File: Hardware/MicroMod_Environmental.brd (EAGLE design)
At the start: 65 x 38 mm, 41 parts, among them J1 MICROMOD_STANDARD, U1 SGP40, U2 EEPROM, U3 SHTC3, U4 3.3V, U5 STC31

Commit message: Adds Silk for default I2C address
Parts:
- added U$10: (no value), top:0X29518
- added U$9: (no value), top:DEFAULT#518
- moved C3 0.05 mm to (25.5, 21.8)
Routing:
- net GND: vias 21 -> 23
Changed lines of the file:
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@@
 <attribute name="VALUE" x="28.321" y="32.766" size="0.6096" layer="27" font="vector" ratio="20" align="top-center"/>
 </element>
-<element name="C3" library="SparkFun-Capacitors" package="0603" value="0.1uF" x="25.5016" y="21.7424" smashed="yes">
-<attribute name="NAME" x="25.5016" y="22.5044" size="0.6096" layer="25" font="vector" ratio="20" align="bottom-center"/>
-<attribute name="PROD_ID" value="CAP-08604" x="25.5016" y="26.8224" size="1.778" layer="27" font="vector" ratio="15" display="off"/>
-<attribute name="VALUE" x="25.5016" y="20.9804" size="0.6096" layer="27" font="vector" ratio="20" align="top-center"/>
+<element name="C3" library="SparkFun-Capacitors" package="0603" value="0.1uF" x="25.5016" y="21.7932" smashed="yes">
+<attribute name="NAME" x="25.5016" y="22.5552" size="0.6096" layer="25" font="vector" ratio="20" align="bottom-center"/>
+<attribute name="PROD_ID" value="CAP-08604" x="25.5016" y="26.8732" size="1.778" layer="27" font="vector" ratio="15" display="off"/>
+<attribute name="VALUE" x="25.5016" y="21.0312" size="0.6096" layer="27" font="vector" ratio="20" align="top-center"/>
 </element>
 <element name="U3" library="SparkFun-Sensors" package="SHTC3" value="SHTC3" x="32.893" y="19.05" smashed="yes" rot="R180">
@@
 <element name="U$7" library="SparkFun-MicroMod" package="MICROMOD_MI_LOGO_1" value="" x="39.116" y="32.512" smashed="yes"/>
 <element name="U$8" library="SparkFun-Buzzard" package="I2C" value="" x="8.001" y="8.255" smashed="yes"/>
+<element name="U$9" library="top" package="DEFAULT#518" value="" x="26.924" y="26.67" smashed="yes"/>
+<element name="U$10" library="top" package="0X29518" value="" x="31.115" y="26.67" smashed="yes"/>
 </elements>
 <signals>
@@
 <via x="43.5102" y="21.6408" extent="1-16" drill="0.3048"/>
 <via x="24.3586" y="17.1958" extent="1-16" drill="0.3048"/>
+<via x="40.5892" y="21.1582" extent="1-16" drill="0.3048"/>
+<via x="37.4142" y="17.018" extent="1-16" drill="0.3048"/>
 </signal>
 <signal name="3.3V" class="2">
@@
 <contactref element="PWR\" pad="2"/>
 <wire x1="32.893" y1="32.893" x2="55.118" y2="32.893" width="0.254" layer="1"/>
-<wire x1="24.6516" y1="21.7424" x2="24.384" y2="21.4748" width="0.3048" layer="1"/>
-<wire x1="24.384" y1="21.4748" x2="24.384" y2="20.828" width="0.3048" layer="1"/>
-<wire x1="24.384" y1="20.828" x2="24.384" y2="20.2" width="0.3048" layer="1"/>
-<wire x1="24.7904" y1="21.8812" x2="24.6516" y2="21.7424" width="0.3048" layer="1"/>
+<wire x1="24.6516" y1="21.7932" x2="24.384" y2="21.5256" width="0.3048" layer="1"/>
+<wire x1="24.384" y1="21.5256" x2="24.384" y2="20.8788" width="0.3048" layer="1"/>
+<wire x1="24.384" y1="20.8788" x2="24.384" y2="20.2" width="0.3048" layer="1"/>
+<wire x1="24.7904" y1="21.932" x2="24.6516" y2="21.7932" width="0.3048" layer="1"/>
 <wire x1="29.3624" y1="20.3454" x2="26.8224" y2="20.3454" width="0.3048" layer="16"/>
 <wire x1="26.8224" y1="20.3454" x2="24.6126" y2="20.3454" width="0.3048" layer="16"/>
@@
 <wire x1="39.3192" y1="18.0349" x2="39.5723" y2="18.288" width="0.3048" layer="1"/>
 <wire x1="39.5723" y1="18.288" x2="40.386" y2="18.288" width="0.3048" layer="1"/>
-<wire x1="24.384" y1="20.828" x2="24.384" y2="20.574" width="0.3048" layer="16"/>
-<via x="24.384" y="20.828" extent="1-16" drill="0.3048"/>
+<wire x1="24.384" y1="20.8788" x2="24.384" y2="20.574" width="0.3048" layer="16"/>
+<via x="24.384" y="20.8788" extent="1-16" drill="0.3048"/>
 <wire x1="24.6126" y1="20.3454" x2="24.384" y2="20.574" width="0.3048" layer="16"/>
 <wire x1="24.13" y1="27.178" x2="24.384" y2="26.924" width="0.3048" layer="16"/>
-<wire x1="24.384" y1="26.924" x2="24.384" y2="20.828" width="0.3048" layer="16"/>
+<wire x1="24.384" y1="26.924" x2="24.384" y2="20.8788" width="0.3048" layer="16"/>
 <via x="38.1" y="19.558" extent="1-16" drill="0.3048"/>
 <wire x1="29.3624" y1="20.3454" x2="30.1498" y2="19.558" width="0.3048" layer="16"/>

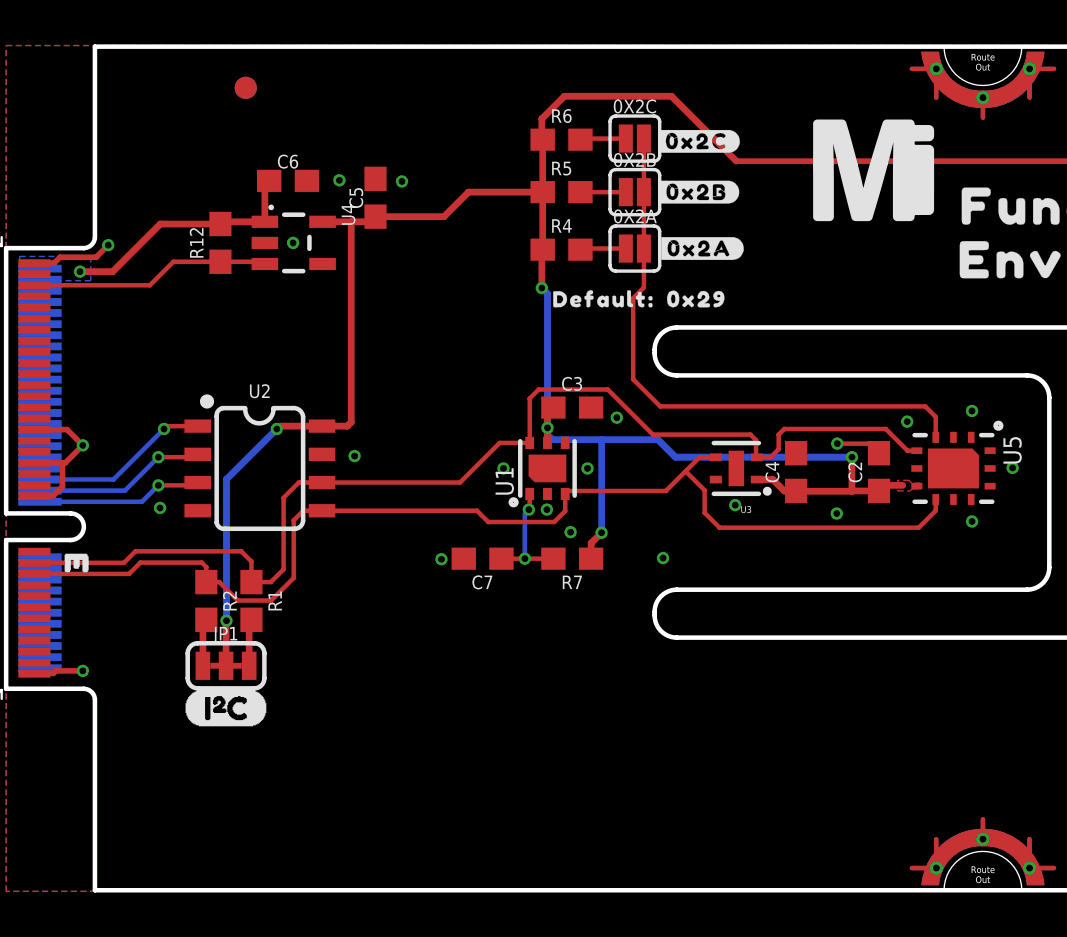
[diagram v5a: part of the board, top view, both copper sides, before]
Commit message: Adds some vias, moves some silk
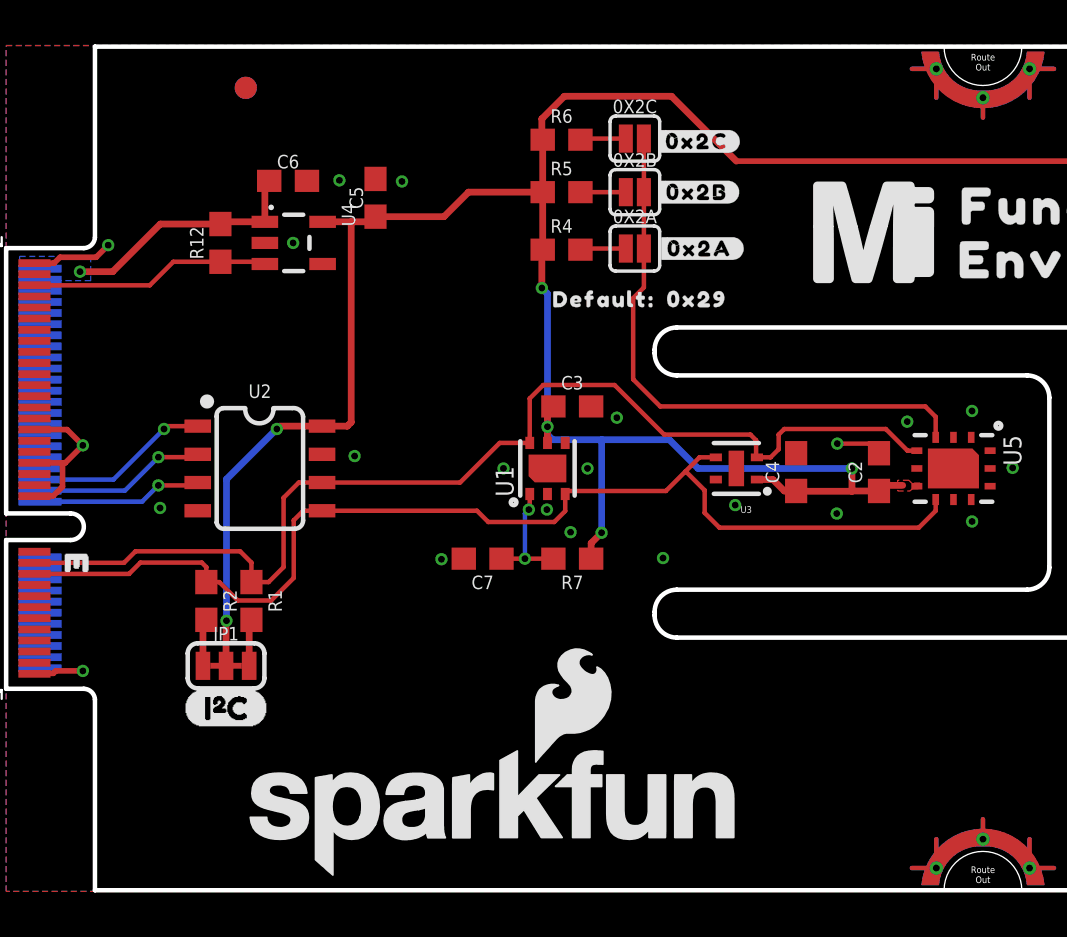
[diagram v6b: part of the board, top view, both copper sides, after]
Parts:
- moved U$7 2.79 mm to (39.1, 29.7)
- moved LOGO1 2.74 mm to (22.0, 3.56), flipped to the top
- moved C3 0.05 mm to (25.5, 21.8)
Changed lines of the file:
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@@
 <?xml version="1.0" encoding="utf-8"?>
 <!DOCTYPE eagle SYSTEM "eagle.dtd">
-<eagle version="9.6.2">
+<eagle version="9.5.1">
 <drawing>
 <settings>
@@
 <setting verticaltext="up"/>
 </settings>
-<grid distance="0.01" unitdist="inch" unit="inch" style="dots" multiple="1" display="yes" altdistance="0.001" altunitdist="inch" altunit="inch"/>
+<grid distance="0.05" unitdist="inch" unit="inch" style="dots" multiple="1" display="yes" altdistance="0.002" altunitdist="inch" altunit="inch"/>
 <layers>
 <layer number="1" name="Top" color="4" fill="1" visible="yes" active="yes"/>
@@
 <attribute name="VALUE" x="28.321" y="32.766" size="0.6096" layer="27" font="vector" ratio="20" align="top-center"/>
 </element>
-<element name="C3" library="SparkFun-Capacitors" package="0603" value="0.1uF" x="25.5016" y="21.7932" smashed="yes">
-<attribute name="NAME" x="25.5016" y="22.5552" size="0.6096" layer="25" font="vector" ratio="20" align="bottom-center"/>
-<attribute name="PROD_ID" value="CAP-08604" x="25.5016" y="26.8732" size="1.778" layer="27" font="vector" ratio="15" display="off"/>
-<attribute name="VALUE" x="25.5016" y="21.0312" size="0.6096" layer="27" font="vector" ratio="20" align="top-center"/>
+<element name="C3" library="SparkFun-Capacitors" package="0603" value="0.1uF" x="25.5016" y="21.844" smashed="yes">
+<attribute name="NAME" x="25.5016" y="22.606" size="0.6096" layer="25" font="vector" ratio="20" align="bottom-center"/>
+<attribute name="PROD_ID" value="CAP-08604" x="25.5016" y="26.924" size="1.778" layer="27" font="vector" ratio="15" display="off"/>
+<attribute name="VALUE" x="25.5016" y="21.082" size="0.6096" layer="27" font="vector" ratio="20" align="top-center"/>
 </element>
 <element name="U3" library="SparkFun-Sensors" package="SHTC3" value="SHTC3" x="32.893" y="19.05" smashed="yes" rot="R180">
@@
 <attribute name="VALUE" x="11.43" y="15.24" size="0.6096" layer="27" font="vector" ratio="20" align="bottom-center"/>
 </element>
-<element name="LOGO1" library="SparkFun-Aesthetics" package="SFE_LOGO_NAME_FLAME_.2" value="SFE_LOGO_NAME_FLAME.2_INCH" x="24.511" y="4.572" smashed="yes" rot="MR0"/>
+<element name="LOGO1" library="SparkFun-Aesthetics" package="SFE_LOGO_NAME_FLAME_.2" value="SFE_LOGO_NAME_FLAME.2_INCH" x="21.971" y="3.556" smashed="yes"/>
 <element name="LOGO2" library="SparkFun-Aesthetics" package="OSHW-LOGO-S" value="OSHW-LOGOS" x="7.62" y="35.052" smashed="yes" rot="MR0"/>
 <element name="FD1" library="SparkFun-Aesthetics" package="FIDUCIAL-1X2" value="FIDUCIAL1X2" x="10.795" y="36.195" smashed="yes"/>
@@
 <element name="U$5" library="top" package="FUNCTION524" value="" x="48.641" y="30.861" smashed="yes"/>
 <element name="U$6" library="top" package="ENVIRONMENTAL526" value="" x="52.451" y="28.448" smashed="yes"/>
-<element name="U$7" library="SparkFun-MicroMod" package="MICROMOD_MI_LOGO_1" value="" x="39.116" y="32.512" smashed="yes"/>
+<element name="U$7" library="SparkFun-MicroMod" package="MICROMOD_MI_LOGO_1" value="" x="39.116" y="29.718" smashed="yes"/>
 <element name="U$8" library="SparkFun-Buzzard" package="I2C" value="" x="8.001" y="8.255" smashed="yes"/>
 <element name="U$9" library="top" package="DEFAULT#518" value="" x="26.924" y="26.67" smashed="yes"/>
@@
 <contactref element="PWR\" pad="2"/>
 <wire x1="32.893" y1="32.893" x2="55.118" y2="32.893" width="0.254" layer="1"/>
-<wire x1="24.6516" y1="21.7932" x2="24.384" y2="21.5256" width="0.3048" layer="1"/>
-<wire x1="24.384" y1="21.5256" x2="24.384" y2="20.8788" width="0.3048" layer="1"/>
-<wire x1="24.384" y1="20.8788" x2="24.384" y2="20.2" width="0.3048" layer="1"/>
-<wire x1="24.7904" y1="21.932" x2="24.6516" y2="21.7932" width="0.3048" layer="1"/>
-<wire x1="29.3624" y1="20.3454" x2="26.8224" y2="20.3454" width="0.3048" layer="16"/>
+<wire x1="24.6516" y1="21.844" x2="24.384" y2="21.5764" width="0.3048" layer="1"/>
+<wire x1="24.384" y1="21.5764" x2="24.384" y2="20.9296" width="0.3048" layer="1"/>
+<wire x1="24.384" y1="20.9296" x2="24.384" y2="20.2" width="0.3048" layer="1"/>
+<wire x1="29.8704" y1="20.3454" x2="26.8224" y2="20.3454" width="0.3048" layer="16"/>
 <wire x1="26.8224" y1="20.3454" x2="24.6126" y2="20.3454" width="0.3048" layer="16"/>
-<wire x1="38.1" y1="19.558" x2="30.1498" y2="19.558" width="0.3048" layer="16"/>
+<wire x1="38.1" y1="19.05" x2="31.1658" y2="19.05" width="0.3048" layer="16"/>
 <wire x1="39.3192" y1="18.0349" x2="39.5723" y2="18.288" width="0.3048" layer="1"/>
 <wire x1="39.5723" y1="18.288" x2="40.386" y2="18.288" width="0.3048" layer="1"/>
-<wire x1="24.384" y1="20.8788" x2="24.384" y2="20.574" width="0.3048" layer="16"/>
-<via x="24.384" y="20.8788" extent="1-16" drill="0.3048"/>
+<wire x1="24.384" y1="20.9296" x2="24.384" y2="20.574" width="0.3048" layer="16"/>
+<via x="24.384" y="20.9296" extent="1-16" drill="0.3048"/>
 <wire x1="24.6126" y1="20.3454" x2="24.384" y2="20.574" width="0.3048" layer="16"/>
 <wire x1="24.13" y1="27.178" x2="24.384" y2="26.924" width="0.3048" layer="16"/>
-<wire x1="24.384" y1="26.924" x2="24.384" y2="20.8788" width="0.3048" layer="16"/>
-<via x="38.1" y="19.558" extent="1-16" drill="0.3048"/>
-<wire x1="29.3624" y1="20.3454" x2="30.1498" y2="19.558" width="0.3048" layer="16"/>
+<wire x1="24.384" y1="26.924" x2="24.384" y2="20.9296" width="0.3048" layer="16"/>
+<via x="38.1" y="19.05" extent="1-16" drill="0.3048"/>
+<wire x1="29.8704" y1="20.3454" x2="31.1658" y2="19.05" width="0.3048" layer="16"/>
 <wire x1="39.3192" y1="18.0349" x2="38.1" y2="18.0349" width="0.3048" layer="1"/>
 <wire x1="38.1" y1="18.0222" x2="38.1" y2="18.0349" width="0.3048" layer="1"/>
-<wire x1="38.1" y1="18.0349" x2="38.1" y2="19.558" width="0.3048" layer="1"/>
+<wire x1="38.1" y1="18.0349" x2="38.1" y2="19.05" width="0.3048" layer="1"/>
 <wire x1="38.1" y1="18.0222" x2="35.5981" y2="18.0222" width="0.3048" layer="1"/>
 <wire x1="35.5981" y1="18.0222" x2="35.5854" y2="18.0349" width="0.3048" layer="1"/>
@@
 <wire x1="12.4968" y1="17.7292" x2="13.1826" y2="18.415" width="0.2032" layer="1"/>
 <wire x1="5.3086" y1="14.8" x2="5.8248" y2="15.3162" width="0.2032" layer="1"/>
-<wire x1="11.049" y1="13.931" x2="11.9244" y2="13.931" width="0.2032" layer="1"/>
-<wire x1="11.9244" y1="13.931" x2="12.4968" y2="14.5034" width="0.2032" layer="1"/>
-<wire x1="12.4968" y1="14.5034" x2="12.4968" y2="17.7292" width="0.2032" layer="1"/>
-<wire x1="11.049" y1="14.859" x2="11.049" y2="13.931" width="0.2032" layer="1"/>
-<wire x1="5.8248" y1="15.3162" x2="10.5918" y2="15.3162" width="0.2032" layer="1"/>
-<wire x1="10.5918" y1="15.3162" x2="11.049" y2="14.859" width="0.2032" layer="1"/>
+<wire x1="11.049" y1="13.931" x2="11.8228" y2="13.931" width="0.2032" layer="1"/>
+<wire x1="12.4968" y1="14.605" x2="11.8228" y2="13.931" width="0.2032" layer="1"/>
+<wire x1="12.4968" y1="14.605" x2="12.4968" y2="17.7292" width="0.2032" layer="1"/>
+<wire x1="11.049" y1="14.8082" x2="11.049" y2="13.931" width="0.2032" layer="1"/>
+<wire x1="5.8248" y1="15.3162" x2="10.541" y2="15.3162" width="0.2032" layer="1"/>
+<wire x1="10.541" y1="15.3162" x2="11.049" y2="14.8082" width="0.2032" layer="1"/>
 <wire x1="41.022" y1="19.85" x2="40.602" y2="19.85" width="0.2032" layer="1"/>
 <wire x1="40.602" y1="19.85" x2="39.624" y2="20.828" width="0.2032" layer="1"/>
@@
 <wire x1="33.782" y1="19.586" x2="33.782" y2="20.32" width="0.2032" layer="1"/>
 <wire x1="33.782" y1="20.32" x2="33.528" y2="20.574" width="0.2032" layer="1"/>
-<wire x1="33.528" y1="20.574" x2="29.1338" y2="20.574" width="0.2032" layer="1"/>
-<wire x1="27.1018" y1="22.606" x2="29.1338" y2="20.574" width="0.2032" layer="1"/>
+<wire x1="33.528" y1="20.574" x2="29.6418" y2="20.574" width="0.2032" layer="1"/>
+<wire x1="27.4066" y1="22.8092" x2="29.6418" y2="20.574" width="0.2032" layer="1"/>
 <wire x1="23.584" y1="20.2" x2="22.232" y2="20.2" width="0.2032" layer="1"/>
 <wire x1="22.232" y1="20.2" x2="20.447" y2="18.415" width="0.2032" layer="1"/>
 <wire x1="20.447" y1="18.415" x2="14.23" y2="18.415" width="0.2032" layer="1"/>
 <wire x1="23.584" y1="20.2" x2="23.584" y2="22.2004875" width="0.2032" layer="1"/>
-<wire x1="23.584" y1="22.2004875" x2="23.9895125" y2="22.606" width="0.2032" layer="1"/>
-<wire x1="23.9895125" y1="22.606" x2="27.1018" y2="22.606" width="0.2032" layer="1"/>
+<wire x1="23.584" y1="22.2004875" x2="24.1927125" y2="22.8092" width="0.2032" layer="1"/>
+<wire x1="24.1927125" y1="22.8092" x2="27.4066" y2="22.8092" width="0.2032" layer="1"/>
 <wire x1="33.818" y1="19.55" x2="34.4344" y2="19.55" width="0.2032" layer="1"/>
 <wire x1="34.4344" y1="19.55" x2="34.798" y2="19.9136" width="0.2032" layer="1"/>
@@
 <wire x1="24.6888" y1="16.637" x2="25.184" y2="17.1322" width="0.2032" layer="1"/>
 <wire x1="25.184" y1="17.9" x2="25.318" y2="18.034" width="0.2032" layer="1"/>
-<wire x1="31.234" y1="19.55" x2="31.4644" y2="19.55" width="0.2032" layer="1"/>
-<wire x1="31.496" y1="19.55" x2="31.968" y2="19.55" width="0.2032" layer="1"/>
 <wire x1="25.318" y1="18.034" x2="29.718" y2="18.034" width="0.2032" layer="1"/>
 <wire x1="29.718" y1="18.034" x2="30.607" y2="18.923" width="0.2032" layer="1"/>
@@
 <wire x1="21.717" y1="16.637" x2="24.6888" y2="16.637" width="0.2032" layer="1"/>
 <wire x1="21.209" y1="17.145" x2="21.717" y2="16.637" width="0.2032" layer="1"/>
-<wire x1="31.4644" y1="19.55" x2="31.496" y2="19.55" width="0" layer="19" extent="1-1"/>
+<wire x1="31.234" y1="19.55" x2="31.968" y2="19.55" width="0.2032" layer="1"/>
 </signal>
 <signal name="ADDR">
